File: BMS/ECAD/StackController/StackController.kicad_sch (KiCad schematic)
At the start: 122 parts, among them Q1 BC846, Q1202 BC846, U1 TLE9012

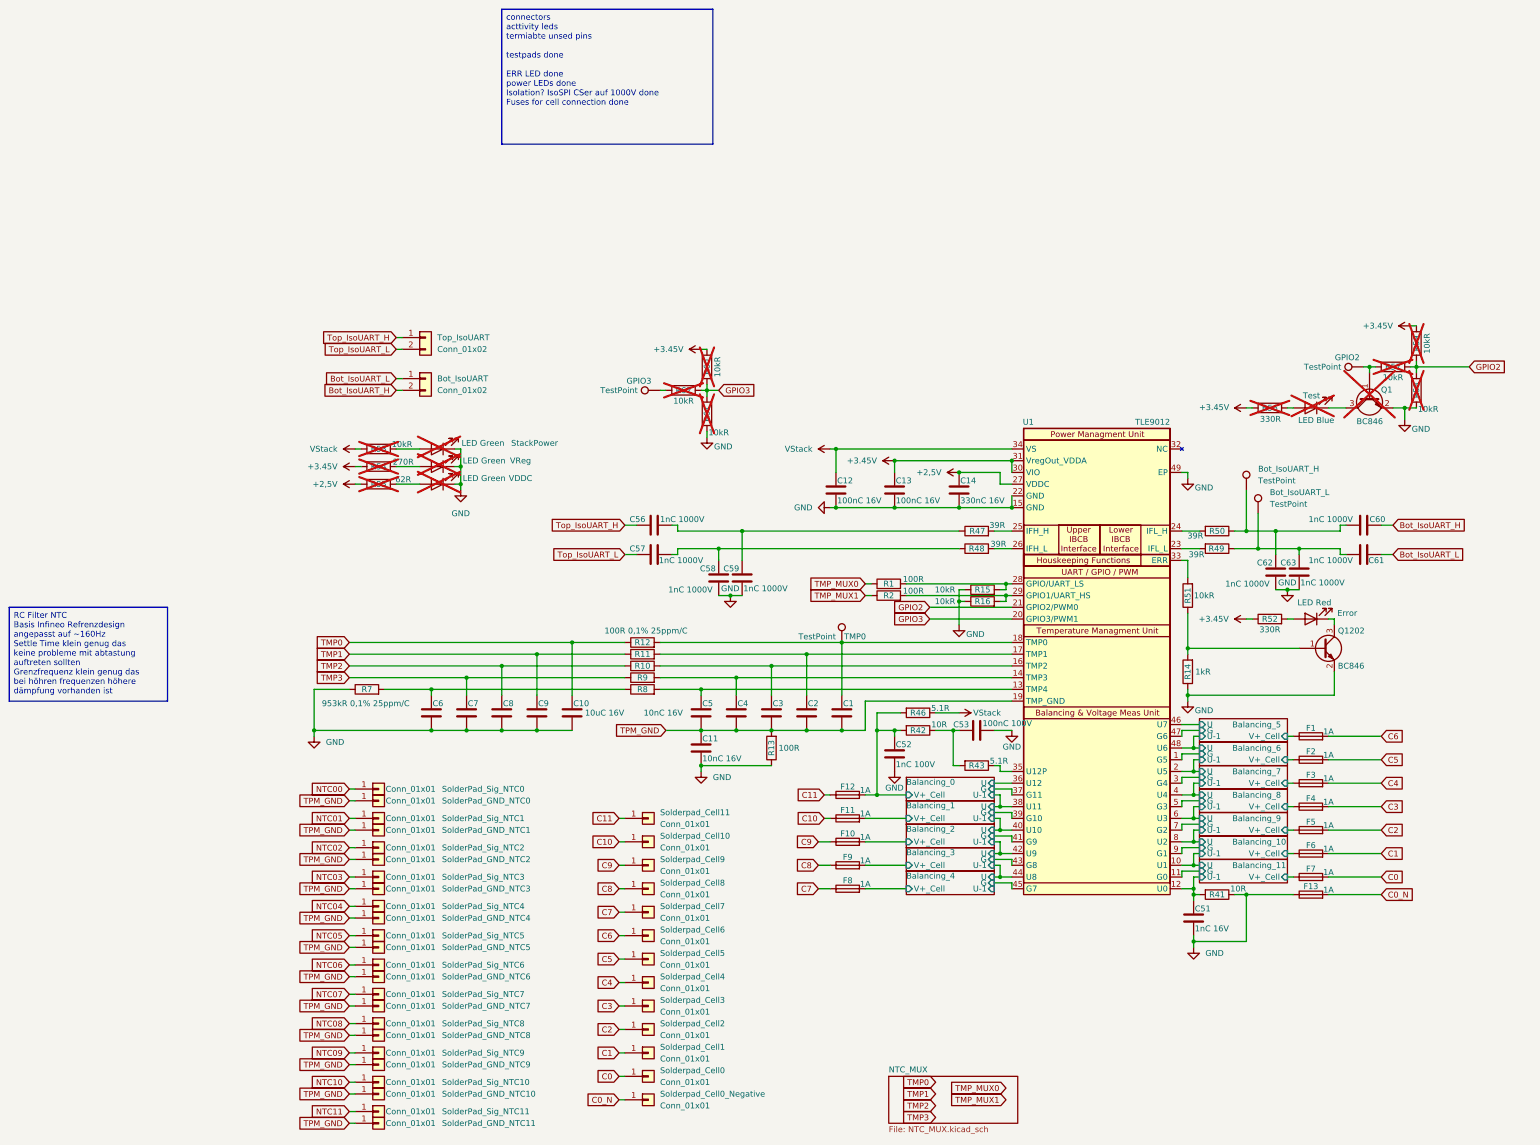
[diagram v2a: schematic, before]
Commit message: started layout BMS slave
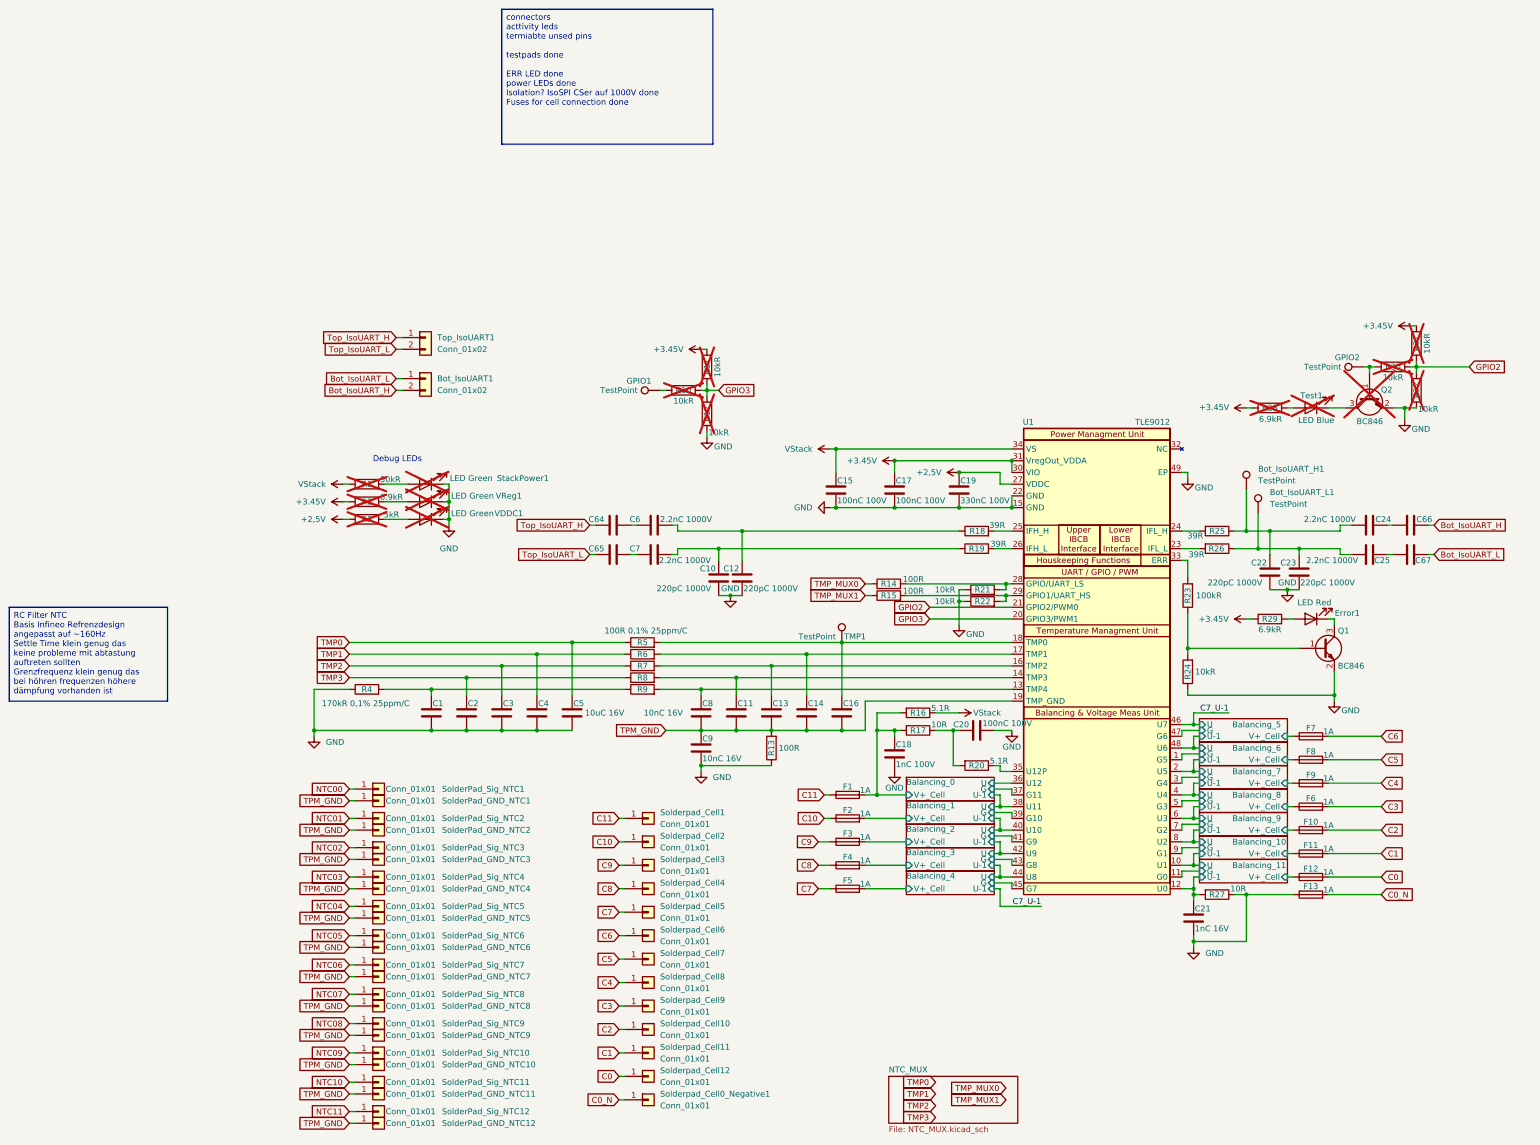
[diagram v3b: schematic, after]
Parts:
- added C64, C65, C66, C67: 2.2nC 1000V, Capacitor_SMD:C_1206_3216Metric, symbol Device:C
- C10: renamed from C58; value 1nC 1000V -> 220pC 1000V
- C12: renamed from C59; value 1nC 1000V -> 220pC 1000V
- C15: renamed from C12; value 100nC 16V -> 100nC 100V
- C17: renamed from C13; value 100nC 16V -> 100nC 100V
- C19: renamed from C14; value 330nC 16V -> 330nC 100V
- C22: renamed from C62; value 1nC 1000V -> 220pC 1000V
- C23: renamed from C63; value 1nC 1000V -> 220pC 1000V
- C24: renamed from C60; value 1nC 1000V -> 2.2nC 1000V
- C25: renamed from C61; value 1nC 1000V -> 2.2nC 1000V
- C5: renamed from C10; footprint Capacitor_SMD:C_0805_2012Metric -> Capacitor_SMD:C_0603_1608Metric
- C6: renamed from C56; value 1nC 1000V -> 2.2nC 1000V
- C7: renamed from C57; value 1nC 1000V -> 2.2nC 1000V
- R1: renamed from R53; value 10kR -> 50kR; footprint Resistor_SMD:R_0805_2012Metric -> Resistor_SMD:R_0603_1608Metric
- R2: renamed from R54; value 270R -> 6.9kR
- R23: renamed from R51; value 10kR -> 100kR
- R24: renamed from R14; value 1kR -> 10kR
- R28: renamed from R56; value 330R -> 6.9kR
- R29: renamed from R52; value 330R -> 6.9kR
- R3: renamed from R55; value 62R -> 5kR
- R4: renamed from R7; value 953kR 0,1% 25ppm/C -> 170kR 0,1% 25ppm/C
- U1: footprint (none) -> Package_QFP:TQFP-48-1EP_7x7mm_P0.5mm_EP5x5mm
- renumbered Bot_IsoUART to Bot_IsoUART1, Bot_IsoUART_H to Bot_IsoUART_H1, Bot_IsoUART_L to Bot_IsoUART_L1, C6 to C1, C4 to C11, C3 to C13, C2 to C14, C1 to C16, C52 to C18, C7 to C2, C53 to C20, C51 to C21, C8 to C3, C9 to C4, C5 to C8, C11 to C9, Error to Error1, F12 to F1, F5 to F10, F6 to F11, F7 to F12, F11 to F2, F10 to F3, F9 to F4, F8 to F5, F4 to F6, F1 to F7, F2 to F8, F3 to F9, GPIO3 to GPIO1, Q1202 to Q1, Q1 to Q2, R62 to R10, R60 to R11, R61 to R12, R1 to R14, R2 to R15, R46 to R16, R42 to R17, R47 to R18, R48 to R19, R43 to R20, R15 to R21, R16 to R22, R50 to R25, R49 to R26, R41 to R27, R57 to R30, R59 to R31, R58 to R32, R12 to R5, R11 to R6, R10 to R7, R9 to R8, R8 to R9, SolderPad_GND_NTC0 to SolderPad_GND_NTC1, SolderPad_GND_NTC9 to SolderPad_GND_NTC10, SolderPad_GND_NTC10 to SolderPad_GND_NTC11, SolderPad_GND_NTC11 to SolderPad_GND_NTC12, SolderPad_GND_NTC1 to SolderPad_GND_NTC2, SolderPad_GND_NTC2 to SolderPad_GND_NTC3, SolderPad_GND_NTC3 to SolderPad_GND_NTC4, SolderPad_GND_NTC4 to SolderPad_GND_NTC5, SolderPad_GND_NTC5 to SolderPad_GND_NTC6, SolderPad_GND_NTC6 to SolderPad_GND_NTC7, SolderPad_GND_NTC7 to SolderPad_GND_NTC8, SolderPad_GND_NTC8 to SolderPad_GND_NTC9, SolderPad_Sig_NTC0 to SolderPad_Sig_NTC1, SolderPad_Sig_NTC9 to SolderPad_Sig_NTC10, SolderPad_Sig_NTC10 to SolderPad_Sig_NTC11, SolderPad_Sig_NTC11 to SolderPad_Sig_NTC12, SolderPad_Sig_NTC1 to SolderPad_Sig_NTC2, SolderPad_Sig_NTC2 to SolderPad_Sig_NTC3, SolderPad_Sig_NTC3 to SolderPad_Sig_NTC4, SolderPad_Sig_NTC4 to SolderPad_Sig_NTC5, SolderPad_Sig_NTC5 to SolderPad_Sig_NTC6, SolderPad_Sig_NTC6 to SolderPad_Sig_NTC7, SolderPad_Sig_NTC7 to SolderPad_Sig_NTC8, SolderPad_Sig_NTC8 to SolderPad_Sig_NTC9, Solderpad_Cell0_Negative to Solderpad_Cell0_Negative1, Solderpad_Cell11 to Solderpad_Cell1, Solderpad_Cell2 to Solderpad_Cell10, Solderpad_Cell1 to Solderpad_Cell11, Solderpad_Cell0 to Solderpad_Cell12, Solderpad_Cell10 to Solderpad_Cell2, Solderpad_Cell9 to Solderpad_Cell3, Solderpad_Cell8 to Solderpad_Cell4, Solderpad_Cell7 to Solderpad_Cell5, Solderpad_Cell5 to Solderpad_Cell7, Solderpad_Cell4 to Solderpad_Cell8, Solderpad_Cell3 to Solderpad_Cell9, StackPower to StackPower1, TMP0 to TMP1, Test to Test1, Top_IsoUART to Top_IsoUART1, VDDC to VDDC1, VReg to VReg1
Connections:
- net Bot_IsoUART_H: now also C66.1; no longer C24.1
- net Bot_IsoUART_L: now also C67.1; no longer C25.1
- net Top_IsoUART_H: now also C64.2; no longer C6.2
- net Top_IsoUART_L: now also C65.2; no longer C7.2
- net Balancing_5/U renamed C7_U-1
- new net: C24.1, C66.2
- new net: C25.1, C67.2
- new net: C6.2, C64.1
- new net: C65.1, C7.2
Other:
- note added: "Debug LEDs"
- moved on the sheet: C22, C24, C25, R1, R2, R3, StackPower1, VDDC1, VReg1
